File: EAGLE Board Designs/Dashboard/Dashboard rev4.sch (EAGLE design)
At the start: 95 parts, among them J1 CONNECTOR-AVR-ISP_2X05_SMD, J2 CONNECTOR-6_μF_S_RA_, J3 CONNECTOR-CAN_μF_S_RA_, J4 CONNECTOR-8_μF_S_RA_, J5 JUMPER_0603_, Q1 TRANSISTOR_N_MOS__PMV15ENEA, Q2 TRANSISTOR_N_MOS__PMV15ENEA, Q3 TRANSISTOR_N_MOS__PMV15ENEA, Q4 TRANSISTOR_N_MOS__PMV15ENEA, Q5 TRANSISTOR_N_MOS__PMV15ENEA, Q6 TRANSISTOR_N_MOS__PMV15ENEA, Q7 TRANSISTOR_N_MOS__PMV15ENEA, U1 ATMEGA328P-AU, U2 RE46C100, U3 MCP23S08, U4 MCP2562FD, U5 MCP2515, X1 CRYSTAL_16MHZ, X2 CRYSTAL_16MHZ

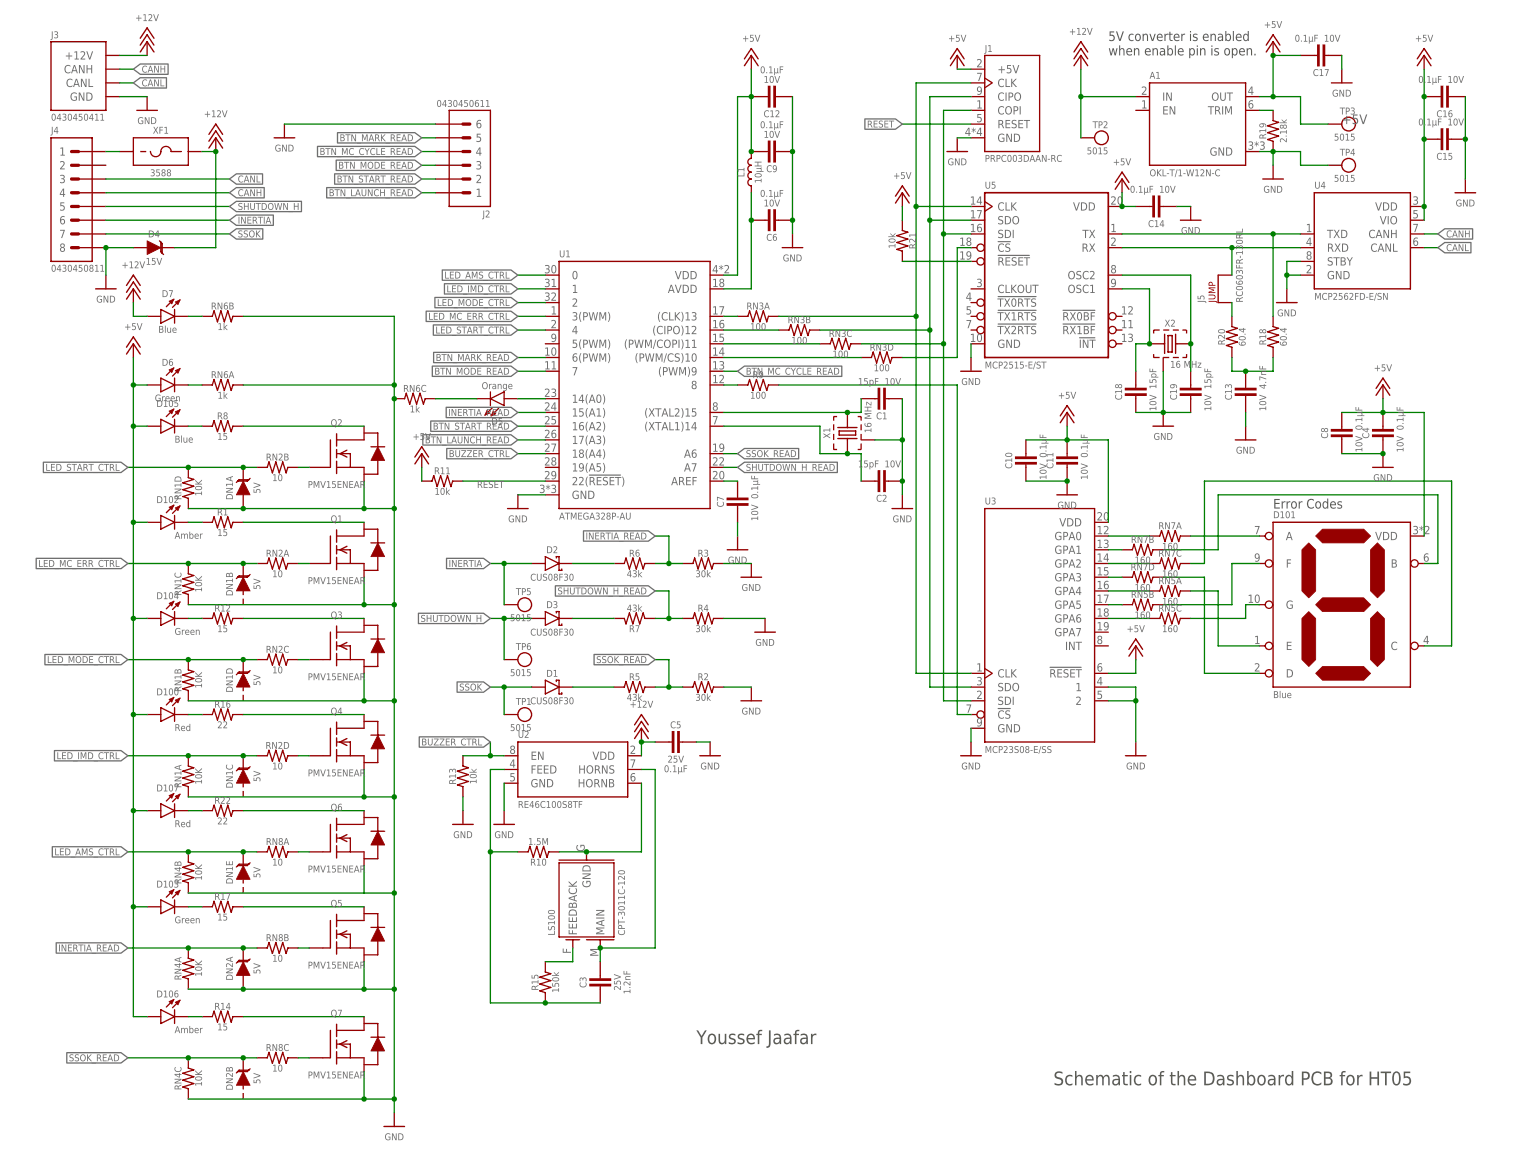
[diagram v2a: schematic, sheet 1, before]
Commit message: Renamed Inertia and SSOK
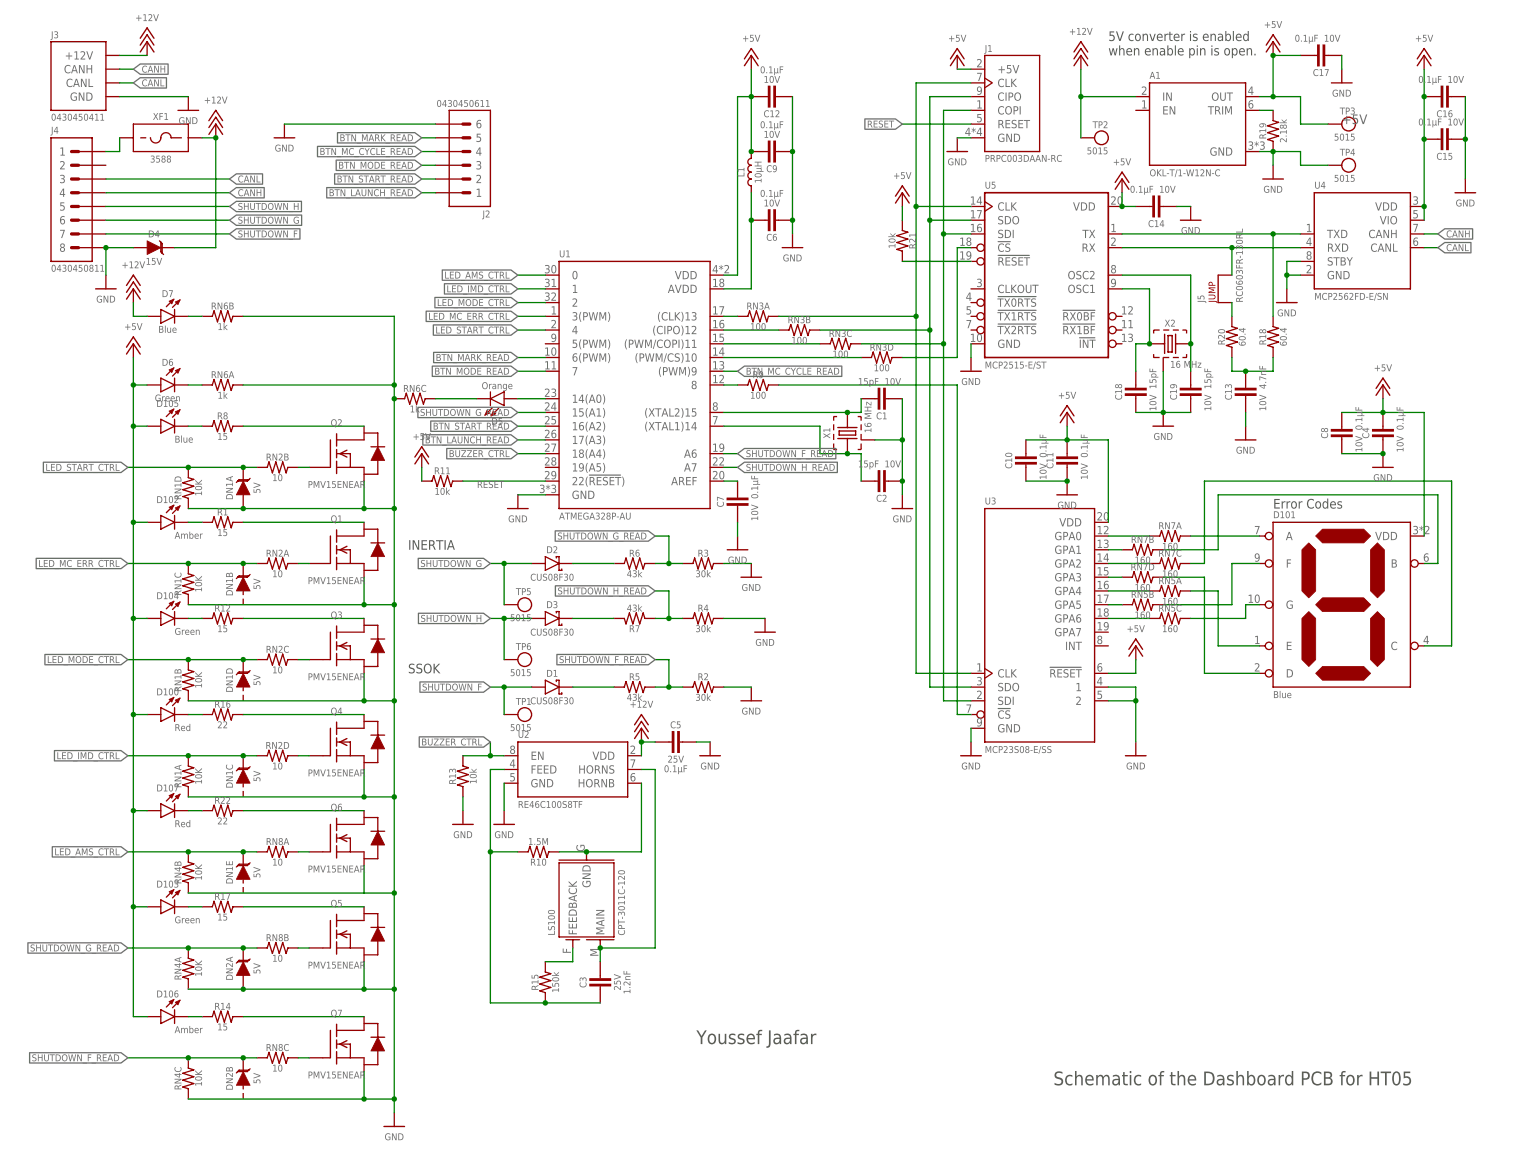
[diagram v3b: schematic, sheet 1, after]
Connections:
- net INERTIA renamed SHUTDOWN_G
- net INERTIA_READ renamed SHUTDOWN_G_READ
- net SSOK renamed SHUTDOWN_F
- net SSOK_READ renamed SHUTDOWN_F_READ
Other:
- note added: "INERTIA"
- note added: "SSOK"
- moved on the sheet: XF1
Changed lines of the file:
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@@
 <text x="205.74" y="205.74" size="1.778" layer="97">5V converter is enabled
 when enable pin is open.</text>
+<text x="76.2" y="91.44" size="1.778" layer="97">SSOK</text>
+<text x="76.2" y="114.3" size="1.778" layer="97">INERTIA</text>
 </plain>
 <instances>
@@
 <attribute name="VALUE" x="20.32" y="161.29" size="1.27" layer="96" align="top-center"/>
 </instance>
-<instance part="P17" gate="1" x="27.94" y="195.58" smashed="yes">
-<attribute name="VALUE" x="27.94" y="194.31" size="1.27" layer="96" align="top-center"/>
+<instance part="P17" gate="1" x="35.56" y="195.58" smashed="yes">
+<attribute name="VALUE" x="35.56" y="194.31" size="1.27" layer="96" align="top-center"/>
 </instance>
 <instance part="P18" gate="1" x="53.34" y="190.5" smashed="yes">
@@
 <attribute name="VALUE" x="25.4" y="154.94" size="1.27" layer="96" align="bottom-center"/>
 </instance>
-<instance part="P36" gate="1" x="40.64" y="190.5" smashed="yes">
-<attribute name="VALUE" x="40.64" y="194.31" size="1.27" layer="96" align="bottom-center"/>
+<instance part="P36" gate="1" x="40.64" y="193.04" smashed="yes">
+<attribute name="VALUE" x="40.64" y="196.85" size="1.27" layer="96" align="bottom-center"/>
 </instance>
 <instance part="P37" gate="1" x="27.94" y="208.28" smashed="yes">
@@
 <attribute name="RESISTANCE" x="130.81" y="87.63" size="1.27" layer="96" align="top-center"/>
 </instance>
-<instance part="XF1" gate="G$1" x="30.48" y="190.5" smashed="yes">
-<attribute name="NAME" x="30.48" y="191.262" size="1.27" layer="95" align="bottom-center"/>
-<attribute name="MPN" x="30.48" y="184.658" size="1.27" layer="96" align="top-center"/>
+<instance part="XF1" gate="G$1" x="30.48" y="193.04" smashed="yes">
+<attribute name="NAME" x="30.48" y="193.802" size="1.27" layer="95" align="bottom-center"/>
+<attribute name="MPN" x="30.48" y="187.198" size="1.27" layer="96" align="top-center"/>
 </instance>
 <instance part="D2" gate="G$1" x="104.14" y="111.76" smashed="yes">
@@
 <segment>
 <pinref part="P17" gate="1" pin="GND"/>
-<wire x1="27.94" y1="198.12" x2="22.86" y2="198.12" width="0.1524" layer="91"/>
+<wire x1="35.56" y1="198.12" x2="22.86" y2="198.12" width="0.1524" layer="91"/>
 <pinref part="J3" gate="G$1" pin="GND"/>
 </segment>
@@
 <pinref part="D4" gate="G$1" pin="C"/>
 <wire x1="33.02" y1="170.18" x2="40.64" y2="170.18" width="0.1524" layer="91"/>
-<wire x1="40.64" y1="170.18" x2="40.64" y2="187.96" width="0.1524" layer="91"/>
+<wire x1="40.64" y1="170.18" x2="40.64" y2="190.5" width="0.1524" layer="91"/>
 <pinref part="P36" gate="1" pin="+12V"/>
 <pinref part="XF1" gate="G$1" pin="2"/>
-<wire x1="40.64" y1="187.96" x2="38.1" y2="187.96" width="0.1524" layer="91"/>
-<junction x="40.64" y="187.96"/>
+<wire x1="40.64" y1="190.5" x2="38.1" y2="190.5" width="0.1524" layer="91"/>
+<junction x="40.64" y="190.5"/>
 </segment>
 <segment>
@@
 </segment>
 </net>
-<net name="SSOK" class="0">
+<net name="SHUTDOWN_F" class="0">
 <segment>
 <wire x1="99.06" y1="88.9" x2="93.98" y2="88.9" width="0.1524" layer="91"/>
@@
 </segment>
 </net>
-<net name="SSOK_READ" class="0">
+<net name="SHUTDOWN_F_READ" class="0">
 <segment>
 <wire x1="121.92" y1="88.9" x2="124.46" y2="88.9" width="0.1524" layer="91"/>
@@
 </segment>
 </net>
-<net name="INERTIA" class="0">
+<net name="SHUTDOWN_G" class="0">
 <segment>
 <wire x1="99.06" y1="111.76" x2="93.98" y2="111.76" width="0.1524" layer="91"/>
@@
 </segment>
 </net>
-<net name="INERTIA_READ" class="0">
+<net name="SHUTDOWN_G_READ" class="0">
 <segment>
 <label x="96.52" y="139.7" size="1.27" layer="95" rot="R180" xref="yes"/>
@@
 </segment>
 </net>
-<net name="N$43" class="0">
-<segment>
-<pinref part="J4" gate="G$1" pin="1"/>
-<pinref part="XF1" gate="G$1" pin="1"/>
-<wire x1="22.86" y1="187.96" x2="20.32" y2="187.96" width="0.1524" layer="91"/>
-</segment>
-</net>
 <net name="N$30" class="0">
 <segment>
@@
 </segment>
 </net>
+<net name="N$43" class="0">
+<segment>
+<pinref part="J4" gate="G$1" pin="1"/>
+<pinref part="XF1" gate="G$1" pin="1"/>
+<wire x1="20.32" y1="187.96" x2="22.86" y2="187.96" width="0.1524" layer="91"/>
+<wire x1="22.86" y1="187.96" x2="22.86" y2="190.5" width="0.1524" layer="91"/>
+</segment>
+</net>
